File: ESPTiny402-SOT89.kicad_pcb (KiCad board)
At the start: 2 copper layers, 26.4 x 23.9 mm, 21 parts, among them J1 Conn_01x10_Male, J2 Conn_01x10_Male, J3 Conn_01x04_Male, U1 ESP-01v090, U2 ATtiny402-SS, U3 MCP1700

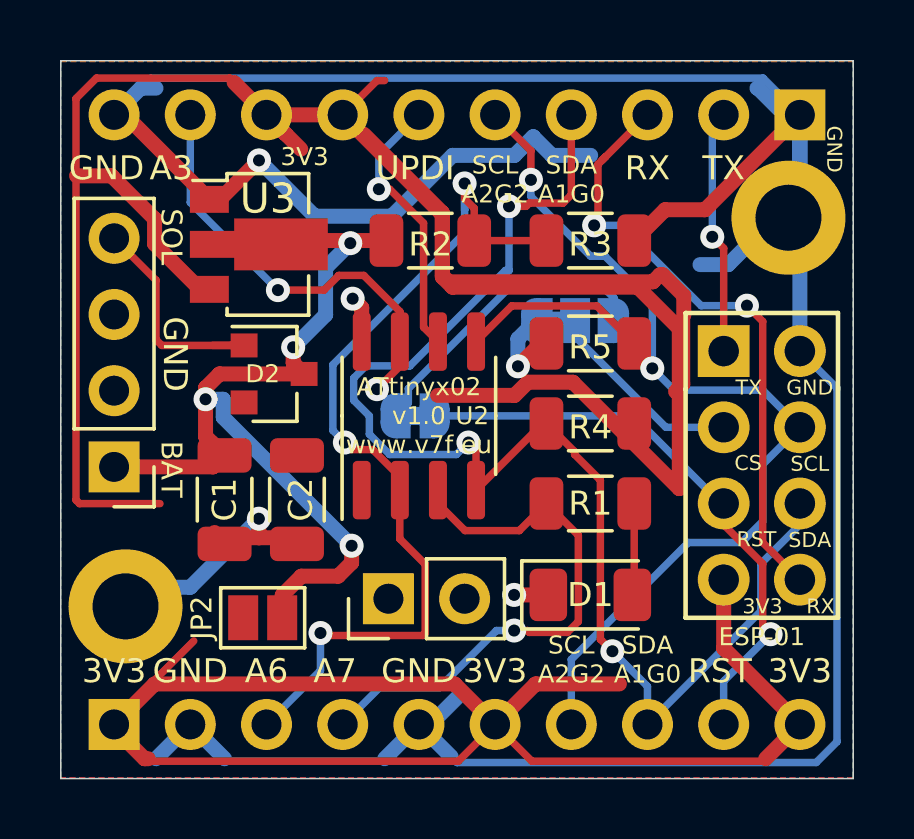
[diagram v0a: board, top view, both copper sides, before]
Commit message: Update 402 layout
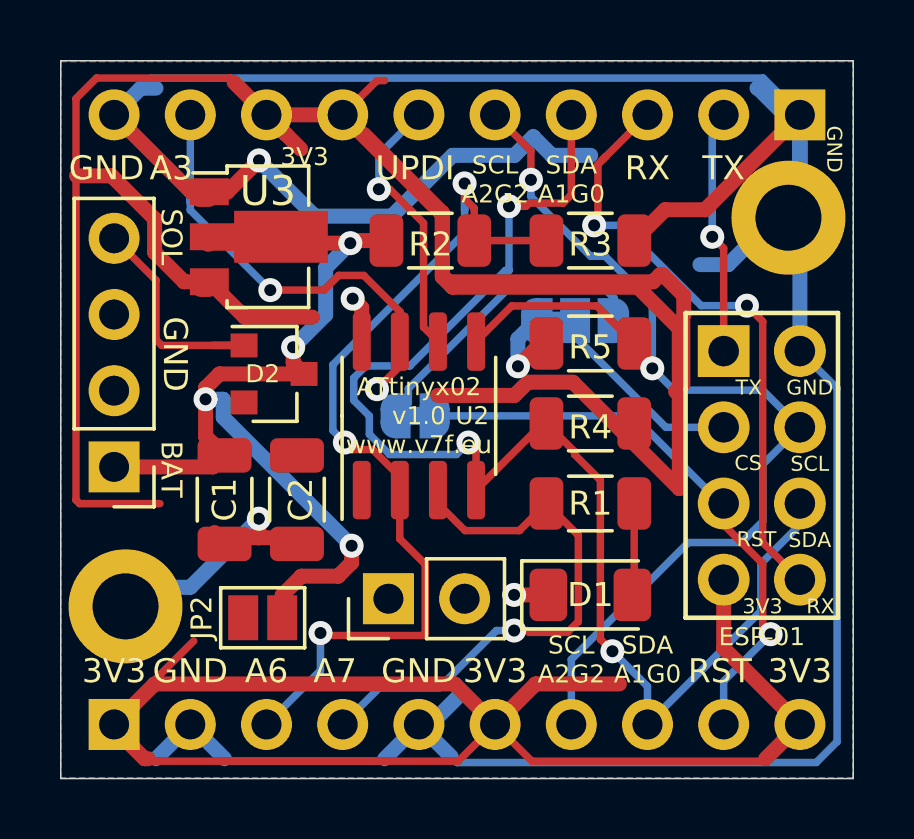
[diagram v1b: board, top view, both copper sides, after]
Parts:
- moved U3 0.25 mm to (52.3, 46.2)
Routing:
- net +3V3: track 141.5 -> 145.8 mm
- net +BATT: track 33.0 -> 33.7 mm
- net GND: track 124.3 -> 124.8 mm
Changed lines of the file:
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@@
     (thickness 1.6)
     (drawings 55)
-    (tracks 327)
+    (tracks 338)
     (zones 0)
     (modules 21)
@@
       (effects (font (size 1 1) (thickness 0.15)))
     )
-    (fp_text user %R (at 0 1.27) (layer F.Fab)
-      (effects (font (size 1 1) (thickness 0.15)))
-    )
     (fp_line (start -0.635 -1.27) (end 1.27 -1.27) (layer F.Fab) (width 0.1))
     (fp_line (start 1.27 -1.27) (end 1.27 3.81) (layer F.Fab) (width 0.1))
@@
     (fp_line (start 1.8 4.35) (end 1.8 -1.8) (layer F.CrtYd) (width 0.05))
     (fp_line (start 1.8 -1.8) (end -1.8 -1.8) (layer F.CrtYd) (width 0.05))
+    (fp_text user %R (at 0 1.27) (layer F.Fab)
+      (effects (font (size 1 1) (thickness 0.15)))
+    )
     (pad 2 thru_hole oval (at 0 2.54 90) (size 1.7 1.7) (drill 1) (layers *.Cu *.Mask))
     (pad 1 thru_hole rect (at 0 0 90) (size 1.7 1.7) (drill 1) (layers *.Cu *.Mask))
@@
   )
   (module Package_TO_SOT_SMD:SOT-89-3 (layer F.Cu)
-    (at 52.324 46.482)
+    (at 52.324 46.228)
     (descr "SOT-89-3, http://ww1.microchip.com/downloads/en/DeviceDoc/3L_SOT-89_MB_C04-029C.pdf")
     (tags SOT-89-3)
@@
   (segment (start 50.849 56.085) (end 50.846999 56.087001) (width 0.5) (layer F.Cu) (net 1) (status 30))
   (via (at 52.324 55.626) (size 0.8) (drill 0.4) (layers F.Cu B.Cu) (net 1))
-  (segment (start 47.856 42.164) (end 50.674 44.982) (width 0.5) (layer F.Cu) (net 1) (status 30))
   (segment (start 47.498 42.164) (end 47.856 42.164) (width 0.5) (layer F.Cu) (net 1) (status 30))
-  (segment (start 51.027206 44.982) (end 52.327612 43.681594) (width 0.5) (layer F.Cu) (net 1) (status 10))
-  (segment (start 50.674 44.982) (end 51.027206 44.982) (width 0.5) (layer F.Cu) (net 1) (status 30))
   (segment (start 47.498 42.164) (end 48.387 41.275) (width 0.5) (layer B.Cu) (net 1) (status 10))
   (segment (start 48.387 41.275) (end 48.895 41.275) (width 0.5) (layer B.Cu) (net 1))
@@
   (segment (start 48.514 57.912) (end 47.879 58.547) (width 0.5) (layer B.Cu) (net 1) (status 30))
   (segment (start 50.038 57.912) (end 48.514 57.912) (width 0.5) (layer B.Cu) (net 1) (status 20))
+  (segment (start 50.674 44.982) (end 50.316 44.982) (width 0.5) (layer F.Cu) (net 1) (status 30))
+  (segment (start 51.281206 44.728) (end 52.327612 43.681594) (width 0.5) (layer F.Cu) (net 1) (status 10))
+  (segment (start 50.674 44.728) (end 51.281206 44.728) (width 0.5) (layer F.Cu) (net 1) (status 30))
+  (segment (start 50.062 44.728) (end 47.498 42.164) (width 0.5) (layer F.Cu) (net 1) (status 30))
+  (segment (start 50.674 44.728) (end 50.062 44.728) (width 0.5) (layer F.Cu) (net 1) (status 30))
   (segment (start 61.9105 49.784) (end 62.1685 49.784) (width 0.5) (layer F.Cu) (net 2) (status 30))
   (segment (start 61.548001 61.133999) (end 60.198 62.484) (width 0.5) (layer F.Cu) (net 2) (status 20))
@@
   (segment (start 56.261 41.021) (end 56.515 41.021) (width 0.25) (layer F.Cu) (net 2))
   (segment (start 52.578 42.164) (end 53.721 43.307) (width 0.5) (layer F.Cu) (net 2) (status 10))
-  (segment (start 47.413202 44.196) (end 46.24501 44.196) (width 0.5) (layer F.Cu) (net 2))
-  (segment (start 48.848001 45.630799) (end 47.413202 44.196) (width 0.5) (layer F.Cu) (net 2))
-  (segment (start 48.848001 46.463125) (end 48.848001 45.630799) (width 0.5) (layer F.Cu) (net 2))
-  (segment (start 50.366876 47.982) (end 48.848001 46.463125) (width 0.5) (layer F.Cu) (net 2) (status 10))
   (segment (start 50.674 47.982) (end 50.366876 47.982) (width 0.5) (layer F.Cu) (net 2) (status 30))
   (segment (start 52.578 42.164) (end 53.227613 42.813613) (width 0.5) (layer F.Cu) (net 2) (status 10))
@@
   (segment (start 70.358 62.484) (end 69.215 63.627) (width 0.5) (layer F.Cu) (net 2) (status 10))
   (segment (start 69.215 63.627) (end 69.132999 63.709001) (width 0.25) (layer F.Cu) (net 2))
+  (segment (start 47.413202 44.196) (end 46.24501 44.196) (width 0.5) (layer F.Cu) (net 2))
+  (segment (start 48.848001 45.630799) (end 47.413202 44.196) (width 0.5) (layer F.Cu) (net 2))
+  (segment (start 48.848001 46.744904) (end 48.848001 45.630799) (width 0.5) (layer F.Cu) (net 2))
+  (segment (start 49.831097 47.728) (end 48.848001 46.744904) (width 0.5) (layer F.Cu) (net 2))
+  (segment (start 50.674 47.728) (end 49.831097 47.728) (width 0.5) (layer F.Cu) (net 2) (status 10))
+  (segment (start 50.674 47.728) (end 50.674 47.753) (width 0.5) (layer F.Cu) (net 2) (status 30))
+  (segment (start 51.852001 48.906001) (end 54.113001 48.906001) (width 0.5) (layer F.Cu) (net 2))
+  (segment (start 50.674 47.728) (end 51.852001 48.906001) (width 0.5) (layer F.Cu) (net 2) (status 10))
   (segment (start 64.8355 58.1035) (end 64.773 58.166) (width 0.25) (layer F.Cu) (net 4) (status 30))
   (segment (start 64.8355 55.118) (end 64.8355 58.1035) (width 0.25) (layer F.Cu) (net 4) (status 30))
   (segment (start 47.498 53.8988) (end 47.498 54.117) (width 0.5) (layer F.Cu) (net 5) (status 30))
   (segment (start 56.4495 46.482) (end 56.5765 46.355) (width 0.5) (layer F.Cu) (net 5) (status 30))
-  (segment (start 56.5765 46.355) (end 51.2695 46.355) (width 0.5) (layer F.Cu) (net 5) (status 30))
   (via (at 55.372 46.441898) (size 0.8) (drill 0.4) (layers F.Cu B.Cu) (net 5))
   (via (at 50.546 51.644598) (size 0.8) (drill 0.4) (layers F.Cu B.Cu) (net 5))
@@
   (segment (start 55.416279 57.092818) (end 54.968087 57.54101) (width 0.5) (layer F.Cu) (net 5))
   (segment (start 55.416279 56.527133) (end 55.416279 57.092818) (width 0.5) (layer F.Cu) (net 5))
+  (segment (start 55.458898 46.355) (end 55.372 46.441898) (width 0.5) (layer F.Cu) (net 5))
+  (segment (start 56.5765 46.355) (end 55.458898 46.355) (width 0.5) (layer F.Cu) (net 5) (status 10))
+  (segment (start 50.674602 46.441898) (end 50.6345 46.482) (width 0.5) (layer F.Cu) (net 5) (status 30))
+  (segment (start 55.372 46.441898) (end 50.674602 46.441898) (width 0.5) (layer F.Cu) (net 5) (status 20))
   (segment (start 59.195532 56.02201) (end 58.293 55.119478) (width 0.25) (layer F.Cu) (net 6) (status 20))
   (segment (start 58.293 55.119478) (end 58.293 54.672) (width 0.25) (layer F.Cu) (net 6) (status 30))
@@
   (segment (start 57.023 50.546) (end 57.023 49.722) (width 0.25) (layer F.Cu) (net 10) (status 30))
   (segment (start 56.261 51.308) (end 57.023 50.546) (width 0.25) (layer F.Cu) (net 10) (status 20))
-  (via (at 52.959 48.006) (size 0.8) (drill 0.4) (layers F.Cu B.Cu) (net 10))
+  (via (at 52.705 48.006) (size 0.8) (drill 0.4) (layers F.Cu B.Cu) (net 10))
   (segment (start 50.038 42.487998) (end 50.038 42.164) (width 0.25) (layer B.Cu) (net 10) (status 30))
   (segment (start 57.023 49.722) (end 57.023 48.747) (width 0.25) (layer F.Cu) (net 10) (status 30))
-  (segment (start 50.038 45.085) (end 52.959 48.006) (width 0.25) (layer B.Cu) (net 10))
-  (segment (start 50.038 42.164) (end 50.038 45.085) (width 0.25) (layer B.Cu) (net 10) (status 10))
   (segment (start 54.986692 47.516154) (end 54.496846 48.006) (width 0.25) (layer F.Cu) (net 10))
-  (segment (start 54.496846 48.006) (end 52.959 48.006) (width 0.25) (layer F.Cu) (net 10))
   (segment (start 55.82214 47.516154) (end 54.986692 47.516154) (width 0.25) (layer F.Cu) (net 10))
   (segment (start 57.023 48.717014) (end 55.82214 47.516154) (width 0.25) (layer F.Cu) (net 10))
   (segment (start 57.023 49.722) (end 57.023 48.717014) (width 0.25) (layer F.Cu) (net 10) (status 10))
+  (segment (start 52.705 48.006) (end 54.496846 48.006) (width 0.25) (layer F.Cu) (net 10))
+  (segment (start 50.038 45.339) (end 50.038 44.958) (width 0.25) (layer B.Cu) (net 10))
+  (segment (start 52.705 48.006) (end 50.038 45.339) (width 0.25) (layer B.Cu) (net 10))
+  (segment (start 50.038 44.958) (end 50.038 45.085) (width 0.25) (layer B.Cu) (net 10))
+  (segment (start 50.038 42.164) (end 50.038 44.958) (width 0.25) (layer B.Cu) (net 10) (status 10))
   (segment (start 62.865 49.552346) (end 62.865 49.022) (width 0.25) (layer B.Cu) (net 11) (status 30))
   (segment (start 65.890654 52.578) (end 62.865 49.552346) (width 0.25) (layer B.Cu) (net 11) (status 20))

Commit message: production 402 SOT89
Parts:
- C1, C2: footprint Capacitor_SMD:C_1206_3216Metric -> Capacitor_SMD:C_1206_3216Metric_Pad1.33x1.80mm_HandSolder
- R1, R2, R3, R4, R5: footprint Resistor_SMD:R_1206_3216Metric -> Resistor_SMD:R_1206_3216Metric_Pad1.30x1.75mm_HandSolder
- moved J3 0.13 mm to (47.6, 53.9)
- moved U3 0.13 mm to (52.3, 46.1)
- moved D2 0.13 mm to (52.8, 50.7)
- moved REF** 0.13 mm to (47.8, 58.5)
- moved REF** 0.13 mm to (70.1, 45.6)
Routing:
- net +3V3: track 145.8 -> 61.8 mm
- net GND: track 124.8 -> 103.8 mm, vias 4 -> 3
- net /A3: track 27.7 -> 26.8 mm
- net /SDA-A1: track 46.2 -> 45.5 mm
- net /SCL-A2: track 38.5 -> 39.1 mm

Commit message: clean up
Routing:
- net GND: track 103.8 -> 103.2 mm
